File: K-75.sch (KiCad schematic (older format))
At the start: 177 parts, among them J1 Conn_01x04, SW1 SW_Push, U1 ATmega32U4-AU, Y1 Crystal_GND24_Small

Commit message: Tracing progress
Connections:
- net COL0: now also U1.1 (PE6)
- net COL1: now also U1.41 (PF0)
- net COL10: now also U1.29 (PB5)
- net COL11: now also U1.28 (PB4)
- net COL12: now also U1.27 (PD7)
- net COL13: now also U1.26 (PD6)
- net COL14: now also U1.25 (PD4)
- net COL2: now also U1.40 (PF1)
- net COL3: now also U1.39 (PF4)
- net COL4: now also U1.38 (PF5)
- net COL5: now also U1.37 (PF6)
- net COL6: now also U1.36 (PF7)
- net COL7: now also U1.32 (PC7)
- net COL8: now also U1.31 (PC6)
- net COL9: now also U1.30 (PB6)
- net ROW0: now also U1.9 (PB1)
- net ROW1: now also U1.10 (PB2)
- net ROW2: now also U1.11 (PB3)
- net ROW3: now also U1.19 (PD1)
- net ROW4: now also U1.18 (PD0)
- net ROW5: now also U1.12 (PB7)
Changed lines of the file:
@@
 Connection ~ 10900 3250
 Connection ~ 10900 5000
+Text GLabel 4750 9450 2    50   Input ~ 0
+COL0
+Text GLabel 4750 9650 2    50   Input ~ 0
+COL1
+Text GLabel 4750 9750 2    50   Input ~ 0
+COL2
+Text GLabel 4750 9850 2    50   Input ~ 0
+COL3
+Text GLabel 4750 9950 2    50   Input ~ 0
+COL4
+Text GLabel 4750 10050 2    50   Input ~ 0
+COL5
+Text GLabel 4750 10150 2    50   Input ~ 0
+COL6
+Text GLabel 4750 8250 2    50   Input ~ 0
+COL7
+Text GLabel 4750 8150 2    50   Input ~ 0
+COL8
+Text GLabel 4750 7850 2    50   Input ~ 0
+COL9
+Text GLabel 4750 7750 2    50   Input ~ 0
+COL10
+Text GLabel 4750 7650 2    50   Input ~ 0
+COL11
+Text GLabel 4750 9150 2    50   Input ~ 0
+COL12
+Text GLabel 4750 9050 2    50   Input ~ 0
+COL13
+Text GLabel 4750 8850 2    50   Input ~ 0
+COL14
+Text GLabel 4750 7350 2    50   Input ~ 0
+ROW0
+Text GLabel 4750 7450 2    50   Input ~ 0
+ROW1
+Text GLabel 4750 7550 2    50   Input ~ 0
+ROW2
+Text GLabel 4750 8550 2    50   Input ~ 0
+ROW3
+Text GLabel 4750 8450 2    50   Input ~ 0
+ROW4
+Text GLabel 4750 7950 2    50   Input ~ 0
+ROW5
 $EndSCHEMATC

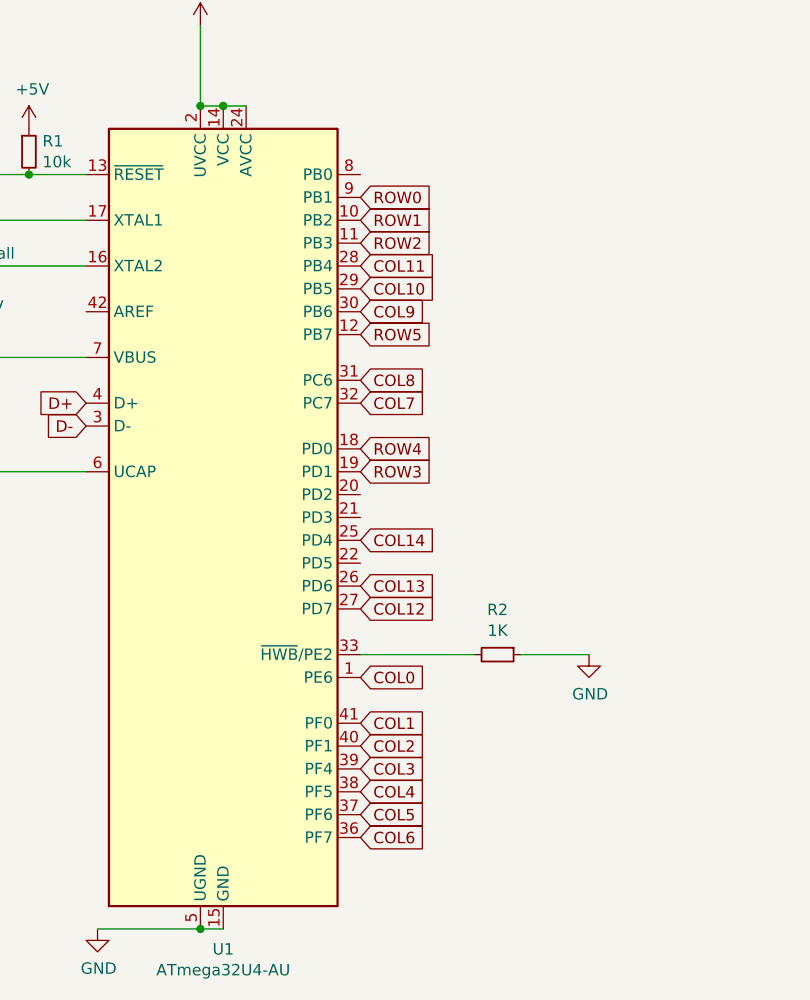
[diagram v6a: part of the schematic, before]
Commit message: Improved routing
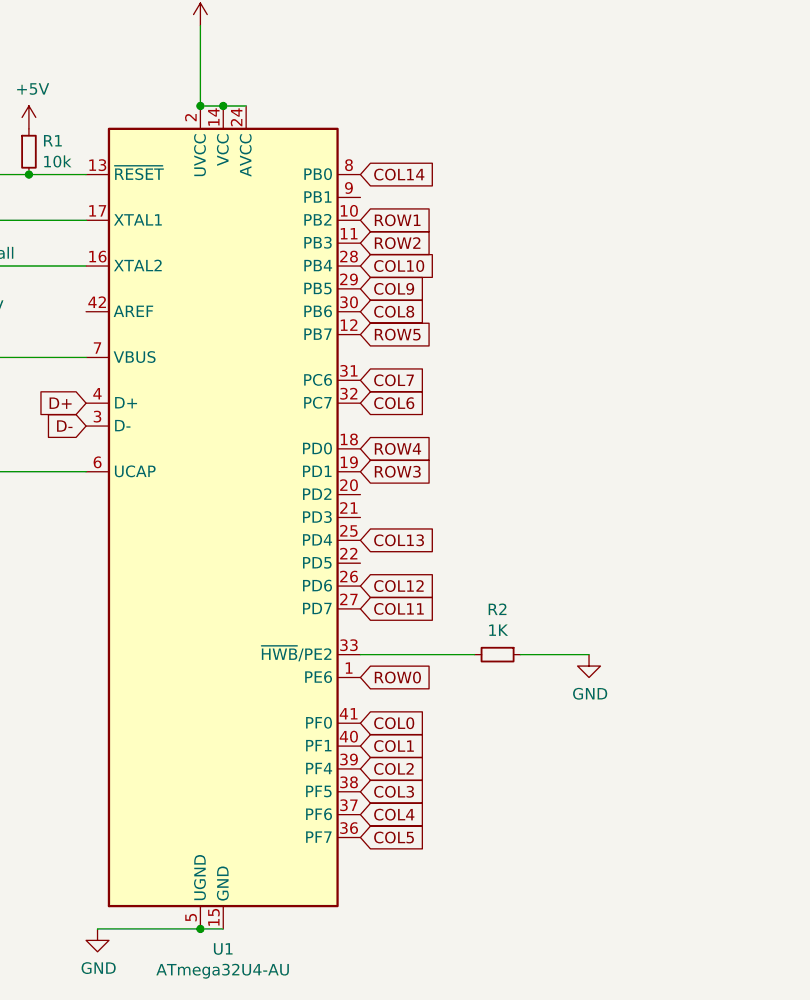
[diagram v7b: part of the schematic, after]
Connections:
- net COL0: now also U1.41 (PF0); no longer U1.1 (PE6)
- net COL1: now also U1.40 (PF1); no longer U1.41 (PF0)
- net COL10: now also U1.28 (PB4); no longer U1.29 (PB5)
- net COL11: now also U1.27 (PD7); no longer U1.28 (PB4)
- net COL12: now also U1.26 (PD6); no longer U1.27 (PD7)
- net COL13: now also U1.25 (PD4); no longer U1.26 (PD6)
- net COL14: now also U1.8 (PB0); no longer U1.25 (PD4)
- net COL2: now also U1.39 (PF4); no longer U1.40 (PF1)
- net COL3: now also U1.38 (PF5); no longer U1.39 (PF4)
- net COL4: now also U1.37 (PF6); no longer U1.38 (PF5)
- net COL5: now also U1.36 (PF7); no longer U1.37 (PF6)
- net COL6: now also U1.32 (PC7); no longer U1.36 (PF7)
- net COL7: now also U1.31 (PC6); no longer U1.32 (PC7)
- net COL8: now also U1.30 (PB6); no longer U1.31 (PC6)
- net COL9: now also U1.29 (PB5); no longer U1.30 (PB6)
- net ROW0: now also U1.1 (PE6); no longer U1.9 (PB1)
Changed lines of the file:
@@
 Connection ~ 10900 3250
 Connection ~ 10900 5000
+Text GLabel 4750 9650 2    50   Input ~ 0
+COL0
+Text GLabel 4750 9750 2    50   Input ~ 0
+COL1
+Text GLabel 4750 9850 2    50   Input ~ 0
+COL2
+Text GLabel 4750 9950 2    50   Input ~ 0
+COL3
+Text GLabel 4750 10050 2    50   Input ~ 0
+COL4
+Text GLabel 4750 10150 2    50   Input ~ 0
+COL5
+Text GLabel 4750 8250 2    50   Input ~ 0
+COL6
+Text GLabel 4750 8150 2    50   Input ~ 0
+COL7
+Text GLabel 4750 7850 2    50   Input ~ 0
+COL8
+Text GLabel 4750 7750 2    50   Input ~ 0
+COL9
+Text GLabel 4750 7650 2    50   Input ~ 0
+COL10
+Text GLabel 4750 9150 2    50   Input ~ 0
+COL11
+Text GLabel 4750 9050 2    50   Input ~ 0
+COL12
+Text GLabel 4750 8850 2    50   Input ~ 0
+COL13
+Text GLabel 4750 7250 2    50   Input ~ 0
+COL14
 Text GLabel 4750 9450 2    50   Input ~ 0
-COL0
-Text GLabel 4750 9650 2    50   Input ~ 0
-COL1
-Text GLabel 4750 9750 2    50   Input ~ 0
-COL2
-Text GLabel 4750 9850 2    50   Input ~ 0
-COL3
-Text GLabel 4750 9950 2    50   Input ~ 0
-COL4
-Text GLabel 4750 10050 2    50   Input ~ 0
-COL5
-Text GLabel 4750 10150 2    50   Input ~ 0
-COL6
-Text GLabel 4750 8250 2    50   Input ~ 0
-COL7
-Text GLabel 4750 8150 2    50   Input ~ 0
-COL8
-Text GLabel 4750 7850 2    50   Input ~ 0
-COL9
-Text GLabel 4750 7750 2    50   Input ~ 0
-COL10
-Text GLabel 4750 7650 2    50   Input ~ 0
-COL11
-Text GLabel 4750 9150 2    50   Input ~ 0
-COL12
-Text GLabel 4750 9050 2    50   Input ~ 0
-COL13
-Text GLabel 4750 8850 2    50   Input ~ 0
-COL14
-Text GLabel 4750 7350 2    50   Input ~ 0
 ROW0
 Text GLabel 4750 7450 2    50   Input ~ 0

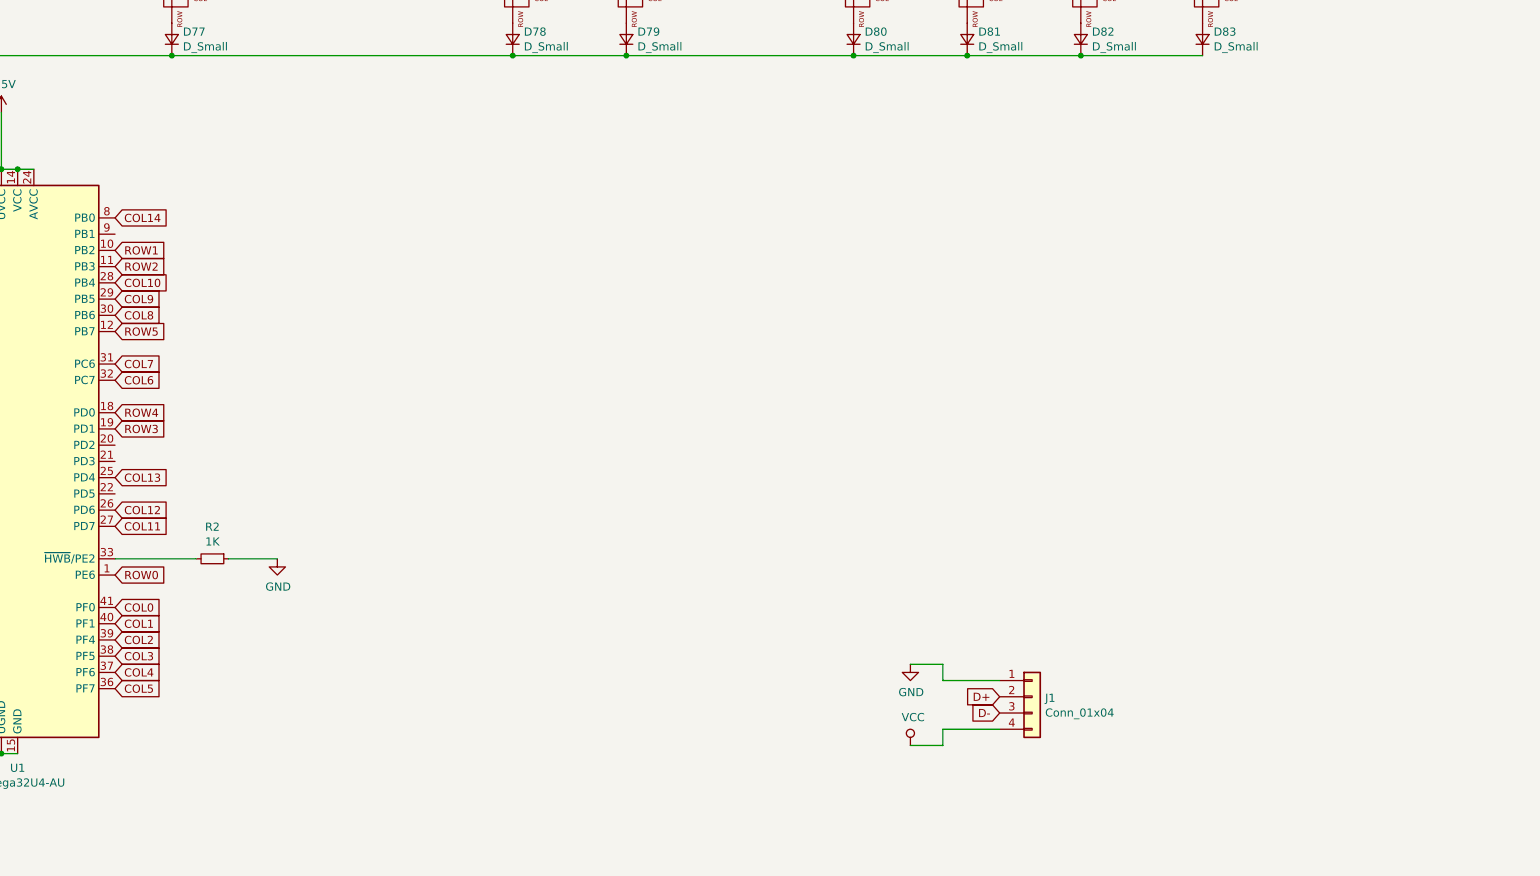
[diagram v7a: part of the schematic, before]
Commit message: Added LEDs
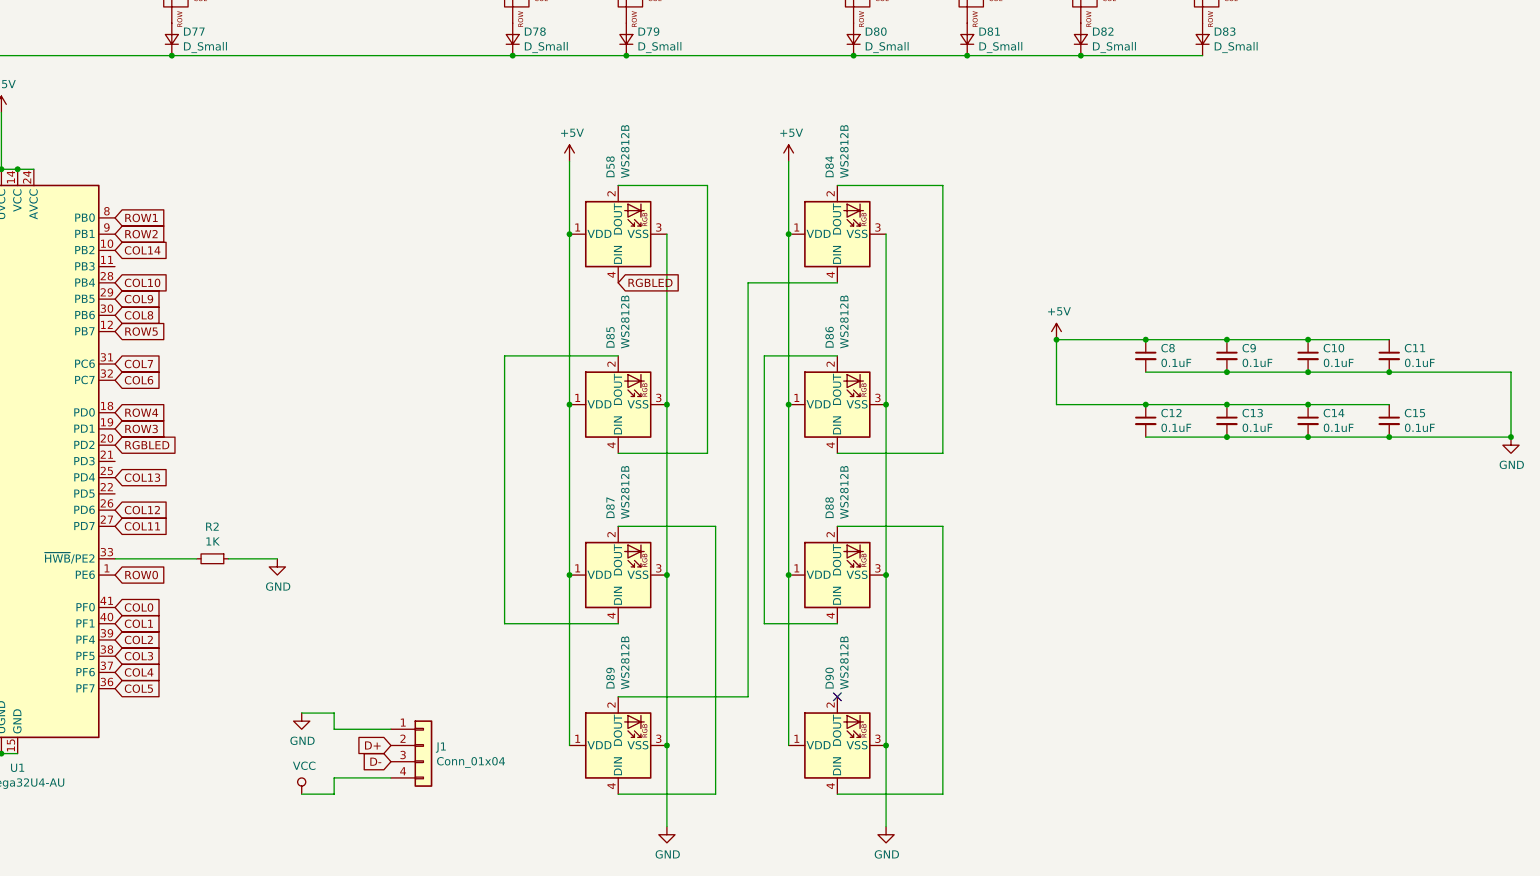
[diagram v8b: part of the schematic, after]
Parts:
- added C10, C11, C12, C13, C14, C15, C8, C9: 0.1uF, Capacitor_SMD:C_0603_1608Metric, symbol Device:C_Small
- added D58, D84, D85, D86, D87, D88, D89, D90: WS2812B, LED_SMD:LED_WS2812B_PLCC4_5.0x5.0mm_P3.2mm, symbol LED:WS2812B
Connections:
- net +5V: now also C10.1, C11.1, C12.1, C13.1, C14.1, C15.1, C8.1, C9.1, D58.1 (VDD), D84.1 (VDD), D85.1 (VDD), D86.1 (VDD), D87.1 (VDD), D88.1 (VDD), D89.1 (VDD), D90.1 (VDD)
- net COL14: now also U1.10 (PB2); no longer U1.8 (PB0)
- net GND: now also C10.2, C11.2, C12.2, C13.2, C14.2, C15.2, C8.2, C9.2, D58.3 (VSS), D84.3 (VSS), D85.3 (VSS), D86.3 (VSS), D87.3 (VSS), D88.3 (VSS), D89.3 (VSS), D90.3 (VSS)
- net ROW1: now also U1.8 (PB0); no longer U1.10 (PB2)
- net ROW2: now also U1.9 (PB1); no longer U1.11 (PB3)
- net RGBLED: now reaches U1.20 (PD2)
- net RGBLED: now also D58.4 (DIN)
- new net: D58.2 (DOUT), D85.4 (DIN)
- new net: D85.2 (DOUT), D87.4 (DIN)
- new net: D87.2 (DOUT), D89.4 (DIN)
- new net: D84.4 (DIN), D89.2 (DOUT)
- new net: D84.2 (DOUT), D86.4 (DIN)
- new net: D86.2 (DOUT), D88.4 (DIN)
- new net: D88.2 (DOUT), D90.4 (DIN)
- no-connect marks 0 -> 1
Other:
- moved on the sheet: J1
